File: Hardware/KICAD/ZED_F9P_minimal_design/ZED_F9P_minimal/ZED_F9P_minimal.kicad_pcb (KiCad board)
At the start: 2 copper layers, 2 parts, among them IC1 ZED-F9P-15B

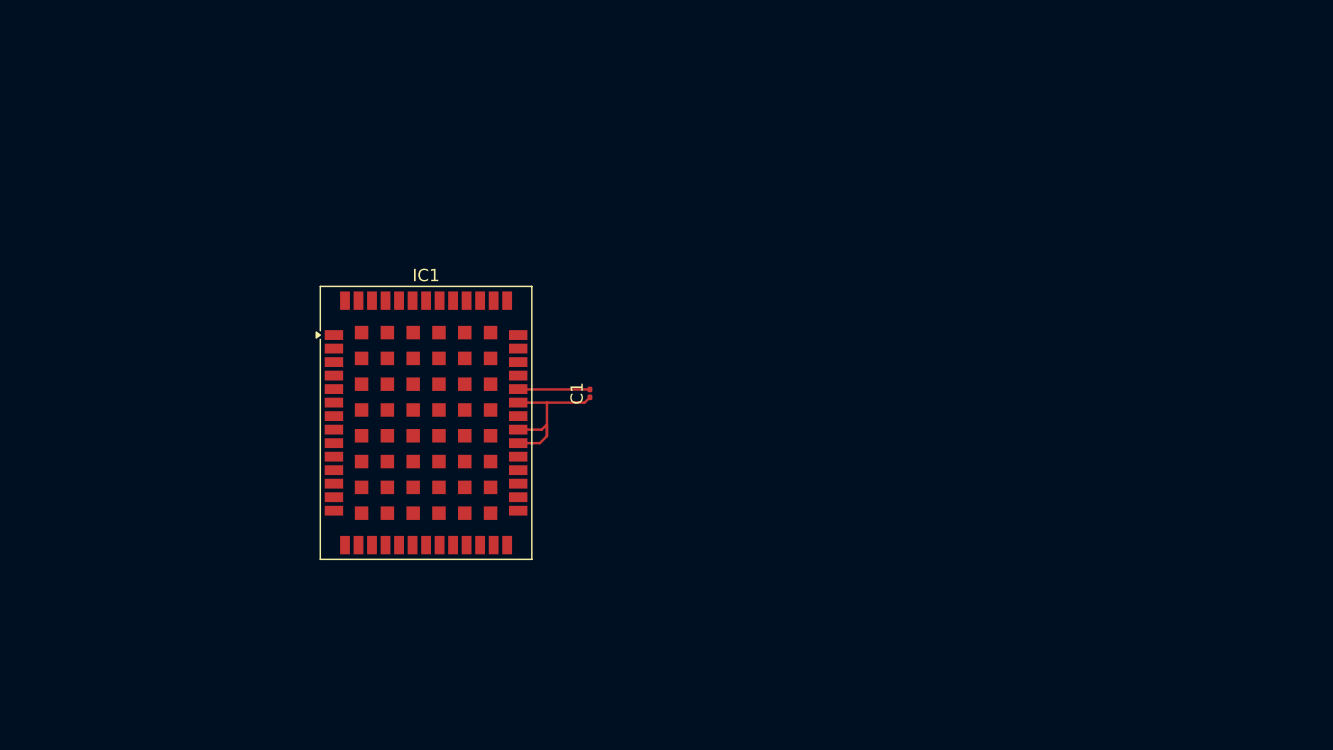
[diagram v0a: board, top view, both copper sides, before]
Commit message: finished adding footprint started PCB layout
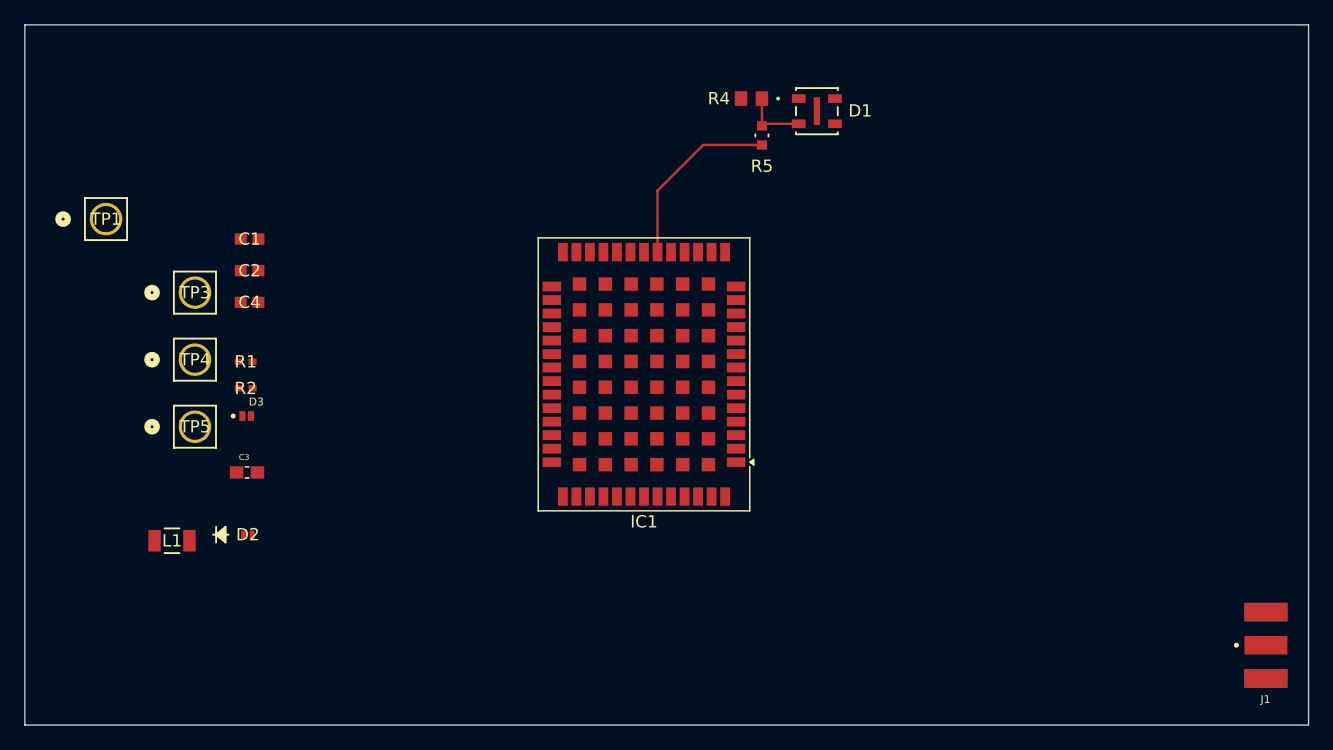
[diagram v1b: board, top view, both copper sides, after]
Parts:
- added C2: 100nf_16V, 0_1uF:YAG_CC0603_YAG, F.Cu at (108.3, 80.5)
- added C3: 11pF, 11pF:CAPC1608X90, F.Cu at (108.1, 96.9)
- added C4: 10µF, 1uF:YAG_CC0603_YAG, F.Cu at (108.3, 83.1)
- added D1: EASR3216RA0, LED_SMD:LED_CREE_MLXXXX, F.Cu at (154.5, 67.5)
- added D2: D_Zener, Diode_SMD:Zener_3.6V, F.Cu at (108.2, 102.0)
- added D3: D_TVS, Diode_SMD:TVS_3.6Vcl, F.Cu at (108.1, 92.3)
- added J1: Conn_Coaxial_Small, SMA:RFSOLUTIONS_CON-SMA-EDGE-S, F.Cu at (191.0, 111.0)
- added L1: 0.01 µH, 0_01uH:STA_RMCF1206_STP, F.Cu at (102.0, 102.5)
- added R1: 10 Ohm, 10_Ohm:RC0402N_YAG, F.Cu at (108.0, 87.9)
- added R2: 8.2ohm, 10_Ohm:RC0402N_YAG, F.Cu at (108.0, 90.1)
- added R4: 120, 120ohm:RC0805N_YAG, F.Cu at (149.1, 66.5)
- added R5: 330, 330_ohm:RC0603N_YAG, F.Cu at (150.0, 69.5)
- added TP1: TestPoint, TestPoint:CONN1_5011_KEY, F.Cu at (96.6, 76.3)
- added TP3: TestPoint, TestPoint:CONN1_5011_KEY, F.Cu at (103.8, 82.3)
- added TP4: TestPoint, TestPoint:CONN1_5011_KEY, F.Cu at (103.8, 87.8)
- added TP5: TestPoint, TestPoint:CONN1_5011_KEY, F.Cu at (103.8, 93.2)
- C1: value 1µF -> 10µF; footprint Capacitor_SMD:C_0201_0603Metric -> 1uF:YAG_CC0603_YAG
- moved C1 30.4 mm to (108.3, 77.9), turned to 0 degrees
- moved IC1 18.2 mm to (140.4, 89.0), turned to 180 degrees
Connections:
- C1 pad 1: +3.3V -> +9V
- IC1 pad 2: /Antenna -> /RF_IN
- IC1 pad 20: unconnected-(IC1-RTK_STAT-Pad20) -> Net-(IC1-RTK_STAT)
- IC1 pad 26: unconnected-(IC1-RXD2-Pad26) -> UART_RX
- IC1 pad 27: unconnected-(IC1-TXD2-Pad27) -> UART_TX
- IC1 pad 33: +3.3V -> Net-(IC1-VCC_1)
- IC1 pad 34: +3.3V -> Net-(IC1-VCC_1)
- IC1 pad 36: +3.3V -> GND
- IC1 pad 39: unconnected-(IC1-USB_DM-Pad39) -> Net-(IC1-USB_DM)
- IC1 pad 40: unconnected-(IC1-USB_DP-Pad40) -> Net-(IC1-USB_DM)
- IC1 pad 53: unconnected-(IC1-TIMEPULSE-Pad53) -> TIMER
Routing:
- net Net-(IC1-RTK_STAT): track 0.00 -> 15.0 mm
- net +3.3V: track 14.8 -> 0.00 mm
- net GND: track 5.85 -> 0.00 mm
- net Net-(D1-A): track 0.00 -> 5.30 mm
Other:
- board outline added: 104.5 x 57 mm

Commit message: finalised first iteration of schematic
schematic 1.0,, gonna start pcb rooting
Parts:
- removed C1: 10µF, 1uF:YAG_CC0603_YAG
- removed C3: 11pF, 11pF:CAPC1608X90
- removed IC1: ZED-F9P-15B, RF_GPS:ublox_ZED
- added C5: 100nF, Capacitor_SMD:C_0805_2012Metric, F.Cu at (135.3, 67.1)
- added C6: 100nF, Capacitor_SMD:C_0805_2012Metric, F.Cu at (135.3, 69.6)
- added J2: DF11-18DS-2DSA06, Connector:CON18_2X9_U_DF11_HIR, F.Cu at (62.1, 92.0)
- added JP1: Jumper_2_Open, Connector:CON_1x02, F.Cu at (134.6, 78.3)
- added JP2: Jumper_2_Open, Connector:CON_1x02, F.Cu at (134.6, 83.6)
- added JP3: Jumper_2_Open, Connector:CON_1x02, F.Cu at (134.6, 88.8)
- added JP4: Jumper_2_Open, Connector:CON_1x02, F.Cu at (134.6, 94.1)
- added R3: 3.9k, res_SMD_4.3kohm:RC0805N_YAG, F.Cu at (140.0, 79.5)
- added R6: 10k, res_SMD_10kohm:YAG_R0805_YAG, F.Cu at (139.4, 67.8)
- added R7: 5.6k, res_SMD_5.6kohm:RC0805N_YAG, F.Cu at (140.0, 88.1)
- added TP2: TestPoint, TestPoint:CONN1_5011_KEY, F.Cu at (108.8, 83.8)
- added U1: OPA2365AID, 00_OPA2365:D8, F.Cu at (120.0, 95.6)
- added U2: LM1086IT-ADJ/NOPB, LM1086:NDE0003B, F.Cu at (112.5, 110.2)
- added U3: ZED-F9P, RF_GPS:ublox_ZED, F.Cu at (87.3, 91.4)
- C2: value 100nf_16V -> 100nf; footprint 0_1uF:YAG_CC0603_YAG -> Capacitor_SMD:C_0805_2012Metric
- C4: footprint 1uF:YAG_CC0603_YAG -> Capacitor_SMD:C_0805_2012Metric
- D1: footprint LED_SMD:LED_CREE_MLXXXX -> LED_SMD:LED_0805_2012Metric
- D2: value D_Zener -> 3.6
- D3: value D_TVS -> 3.7; footprint Diode_SMD:TVS_3.6Vcl -> Diode_SMD:D_SOD962_TVS_3.7V
- L1: footprint 0_01uH:STA_RMCF1206_STP -> Inductor_SMD:L_0805_2012Metric
- R1: footprint 10_Ohm:RC0402N_YAG -> res_SMD_330ohm:RC0805N_YAG
- R2: value 8.2ohm -> 10k; footprint 10_Ohm:RC0402N_YAG -> res_SMD_10kohm:YAG_R0805_YAG
- R4: footprint 120ohm:RC0805N_YAG -> res_SMD_120ohm:RC0805N_YAG
- R5: footprint 330_ohm:RC0603N_YAG -> res_SMD_330ohm:RC0805N_YAG
- moved D2 58.2 mm to (152.7, 64.5)
- moved L1 56.4 mm to (143.8, 64.6)
- moved D3 48.8 mm to (151.3, 69.7)
- moved R2 40.4 mm to (139.4, 64.7)
- moved C4 38.6 mm to (143.6, 67.3)
- moved R1 33.9 mm to (140.0, 76.7)
- moved C2 31.4 mm to (135.3, 64.5)
- moved R5 18.7 mm to (140.0, 85.3), turned to 0 degrees
- moved J1 18.5 mm to (173.0, 115.1), turned to 0 degrees
- moved R4 18.4 mm to (140.0, 82.4), turned to 0 degrees
- moved TP1 12.3 mm to (108.8, 78.3)
- moved TP3 8.50 mm to (108.8, 89.2)
- moved TP4 8.50 mm to (108.8, 94.7)
- moved TP5 8.50 mm to (108.8, 100.1)
- moved D1 3.01 mm to (151.5, 67.2)
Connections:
- C4 pad 1: Net-(IC1-VCC_1) -> /3v3_puce
- R1 pad 1: Net-(IC1-VCC_1) -> Net-(C2-Pad1)
- R1 pad 2: Net-(C2-Pad1) -> /5v_antenne
- R2 pad 1: /RF_IN -> Net-(U2-OUTPUT)
- R2 pad 2: /RF_IN -> /3V3-IN
- TP4 pad 1: Net-(IC1-VCC_1) -> /3v3_puce
- TP5 pad 1: GND -> /5V-IN
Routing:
- net Net-(U3-RTK_STAT): track 15.0 -> 0.00 mm
- net Net-(D1-A): track 5.30 -> 0.00 mm
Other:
- board outline removed

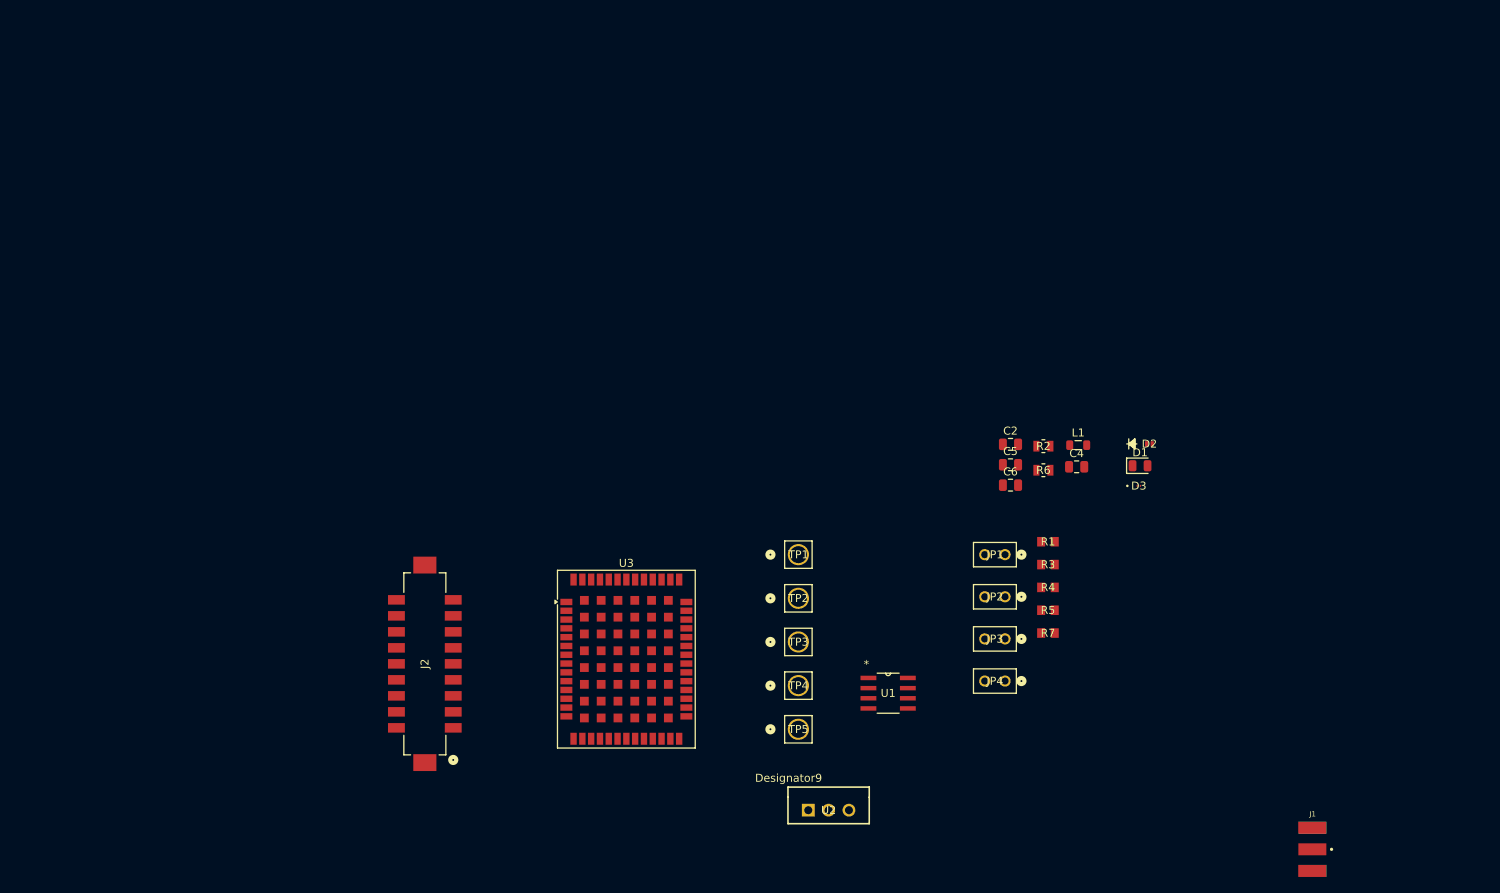
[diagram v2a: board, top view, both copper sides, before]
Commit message: changed diode footprint
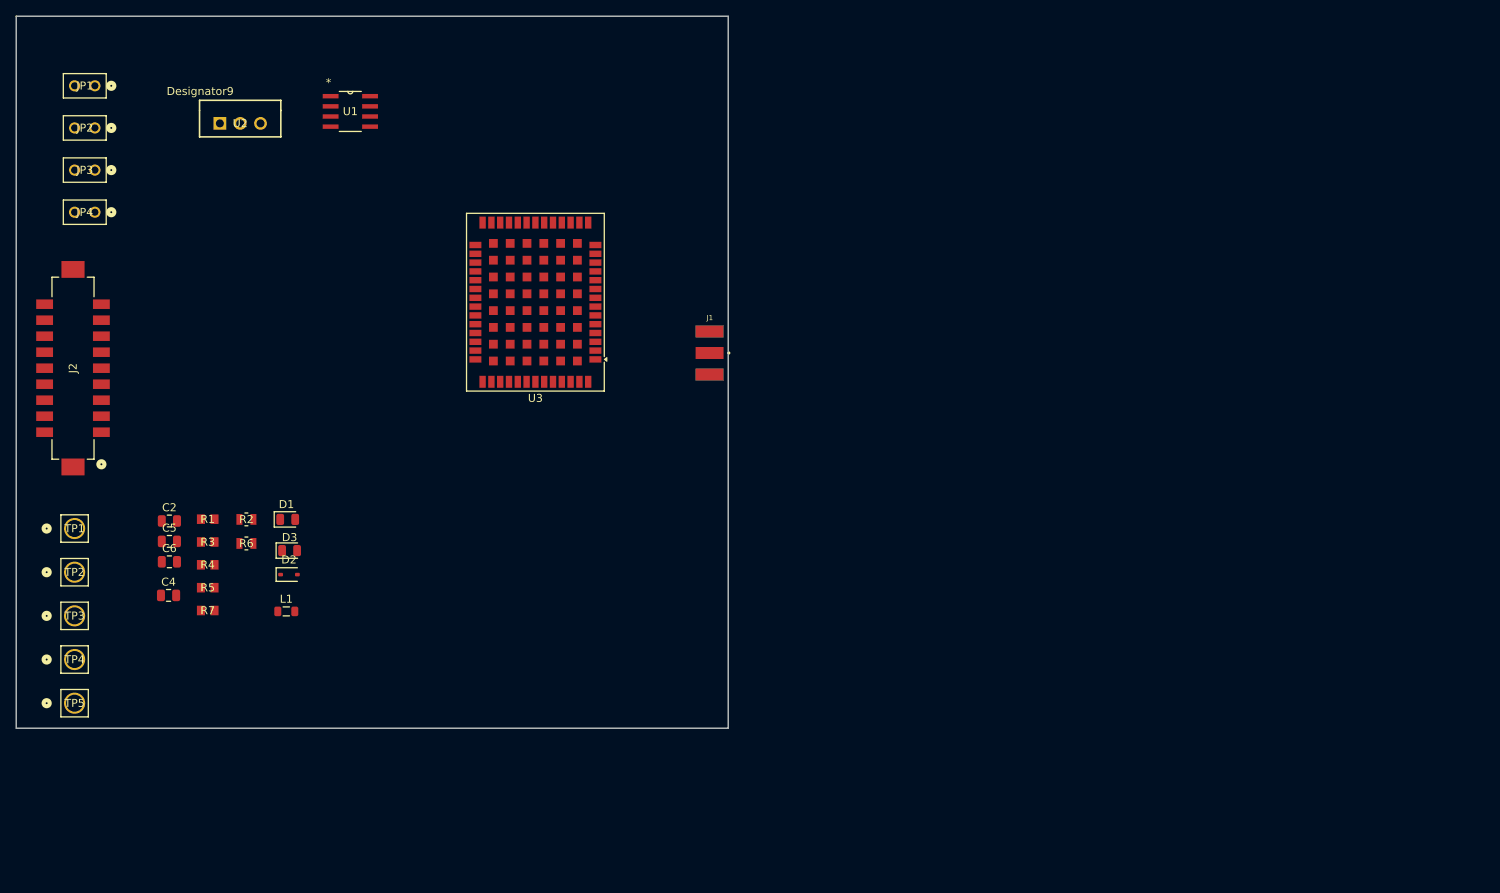
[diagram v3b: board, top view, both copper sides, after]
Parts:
- D1: value EASR3216RA0 -> LED_rouge
- D2: footprint Diode_SMD:Zener_3.6V -> Diode_SMD:D_SOD-323
- D3: footprint Diode_SMD:D_SOD962_TVS_3.7V -> Diode_SMD:D_0805_2012Metric
- moved JP1 128.0 mm to (20.8, 19.7)
- moved JP2 128.0 mm to (20.8, 25.0)
- moved JP3 128.0 mm to (20.8, 30.2)
- moved JP4 128.0 mm to (20.8, 35.5)
- moved C4 114.6 mm to (30.0, 83.4)
- moved U2 113.0 mm to (39.0, 24.4)
- moved D2 108.8 mm to (45.1, 80.8)
- moved D1 106.8 mm to (44.9, 73.9)
- moved D3 106.5 mm to (45.2, 77.8)
- moved C2 105.6 mm to (30.1, 74.1)
- moved C5 105.6 mm to (30.1, 76.6)
- moved C6 105.6 mm to (30.1, 79.2)
- moved R1 105.1 mm to (34.9, 73.9)
- moved R3 105.1 mm to (34.9, 76.7)
- moved R4 105.1 mm to (34.9, 79.6)
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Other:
- board outline added: 89 x 89 mm

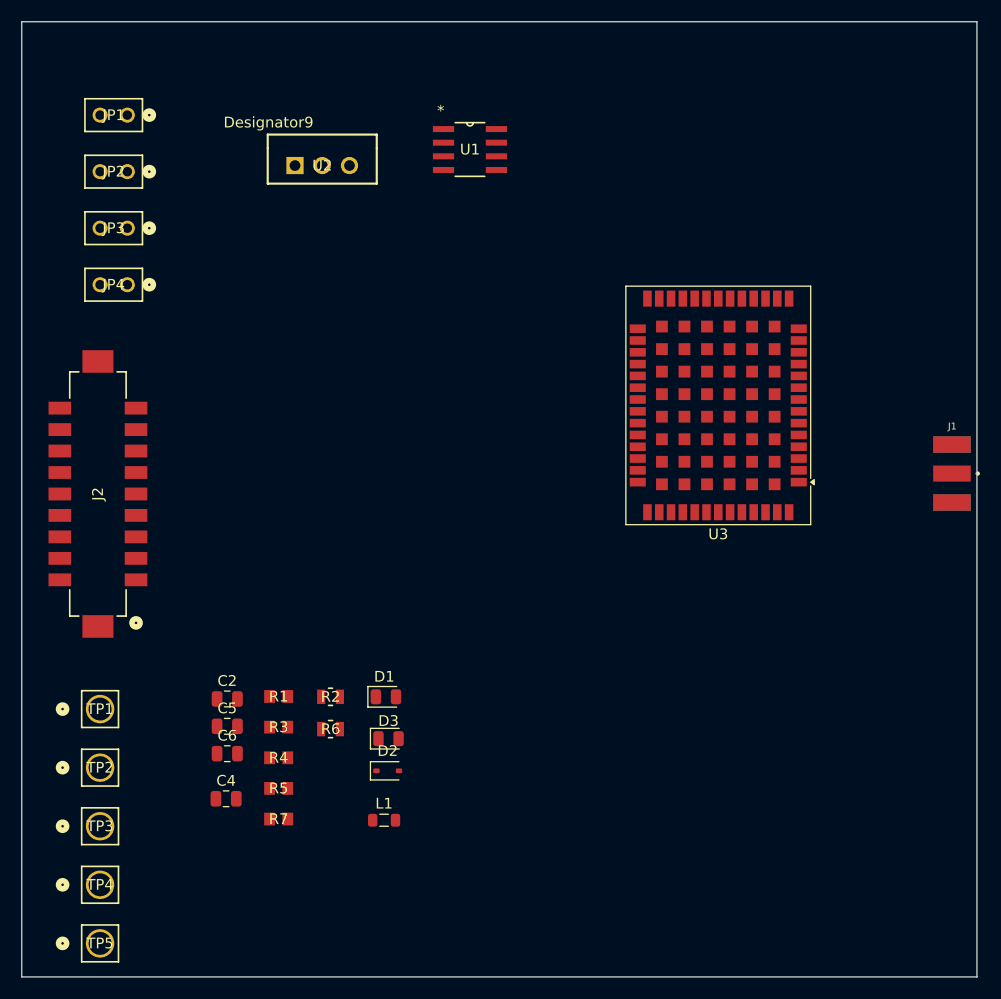
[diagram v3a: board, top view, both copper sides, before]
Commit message: Z9P PCB
arranged placement, rooting still to do
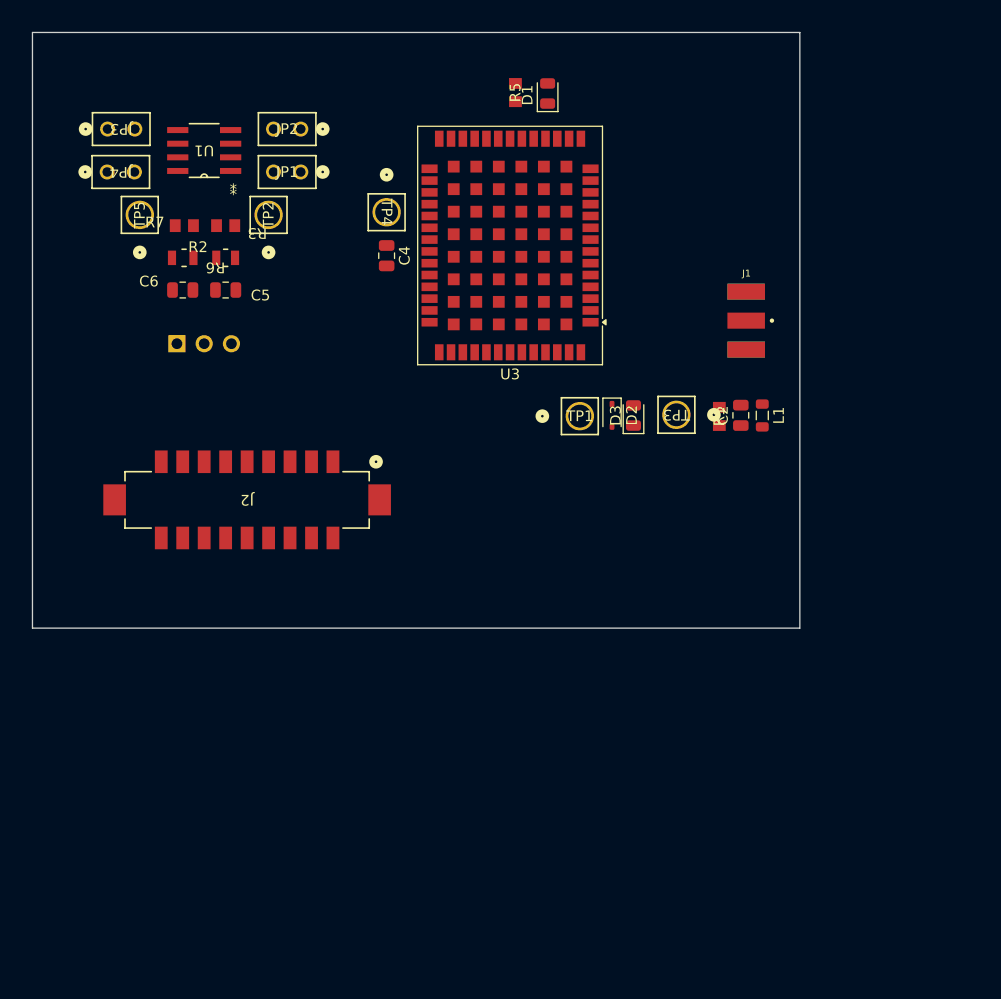
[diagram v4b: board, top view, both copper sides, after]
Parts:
- removed R4: 120, res_SMD_120ohm:RC0805N_YAG
- U2: moved to B.Cu
- moved R5 68.5 mm to (57.0, 17.6), turned to 90 degrees
- moved TP4 68.1 mm to (45.0, 28.8), turned to -90 degrees
- moved TP5 68.0 mm to (22.0, 29.0), turned to 90 degrees
- moved TP3 66.0 mm to (72.0, 47.6), turned to 180 degrees
- moved D1 58.2 mm to (60.0, 17.7), turned to 90 degrees
- moved R7 56.0 mm to (26.2, 30.0)
- moved C2 54.7 mm to (78.0, 47.7), turned to 90 degrees
- moved TP2 53.8 mm to (34.0, 29.0), turned to 90 degrees
- moved C4 52.8 mm to (45.0, 32.8), turned to -90 degrees
- moved TP1 52.4 mm to (63.0, 47.8)
- moved L1 51.6 mm to (80.0, 47.7), turned to -90 degrees
- moved R1 48.7 mm to (76.0, 47.8), turned to 90 degrees
- moved R3 47.0 mm to (30.0, 30.0), turned to 180 degrees
- moved R6 46.0 mm to (26.1, 33.0), turned to 180 degrees
- moved C6 43.4 mm to (26.0, 36.0)
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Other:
- board size 89 x 89 mm -> 71.5 x 55.5 mm

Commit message: rooting pcb
work in progerss
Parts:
- moved JP4 52.6 mm to (71.2, 30.9), turned to 90 degrees
- moved JP3 49.3 mm to (67.2, 30.9), turned to 90 degrees
- moved JP2 44.2 mm to (71.2, 48.9), turned to -90 degrees
- moved U1 43.8 mm to (68.4, 40.1), turned to 90 degrees
- moved TP5 41.1 mm to (63.0, 31.4), turned to 0 degrees
- moved D1 38.7 mm to (22.1, 25.4), turned to 180 degrees
- moved JP1 38.6 mm to (67.2, 48.9), turned to -90 degrees
- moved R7 37.0 mm to (62.2, 38.1), turned to -90 degrees
- moved R5 36.6 mm to (22.0, 28.4), turned to 180 degrees
- moved TP2 34.8 mm to (63.2, 47.9), turned to 0 degrees
- moved R3 34.4 mm to (62.2, 41.9), turned to 90 degrees
- moved R6 33.5 mm to (59.2, 38.1), turned to 90 degrees
- moved R2 30.6 mm to (59.2, 41.9), turned to -90 degrees
- moved C6 30.3 mm to (56.2, 37.9), turned to -90 degrees
- moved TP3 29.2 mm to (59.3, 21.4), turned to 0 degrees
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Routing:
- net /3v3_puce: track 0.00 -> 49.8 mm, vias 0 -> 4
- net /RF_IN: track 0.00 -> 33.3 mm
- net Net-(U2-OUTPUT): track 0.00 -> 24.2 mm
- net /TIMER: track 0.00 -> 23.7 mm
- net /12V: track 0.00 -> 21.0 mm, vias 0 -> 2
- net /I_RESET: track 0.00 -> 18.9 mm
- net /I_D_Sel: track 0.00 -> 16.1 mm
- net /5v_antenne: track 0.00 -> 16.0 mm, vias 0 -> 2
- net /O_TX_STATE: track 0.00 -> 14.6 mm
- net /5V-IN: track 0.00 -> 13.6 mm
- net /I/O_CLK_SELECT: track 0.00 -> 13.1 mm
- net /3V3-IN: track 0.00 -> 13.0 mm
- net GND: track 0.00 -> 12.0 mm
- net /I/O : track 0.00 -> 11.4 mm
- net /UART_RX: track 0.00 -> 9.67 mm
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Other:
- board size 71.5 x 55.5 mm -> 65.2 x 44.5 mm
